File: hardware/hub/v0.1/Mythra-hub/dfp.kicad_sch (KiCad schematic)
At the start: 3 parts, among them J3 918-418K2022C40000

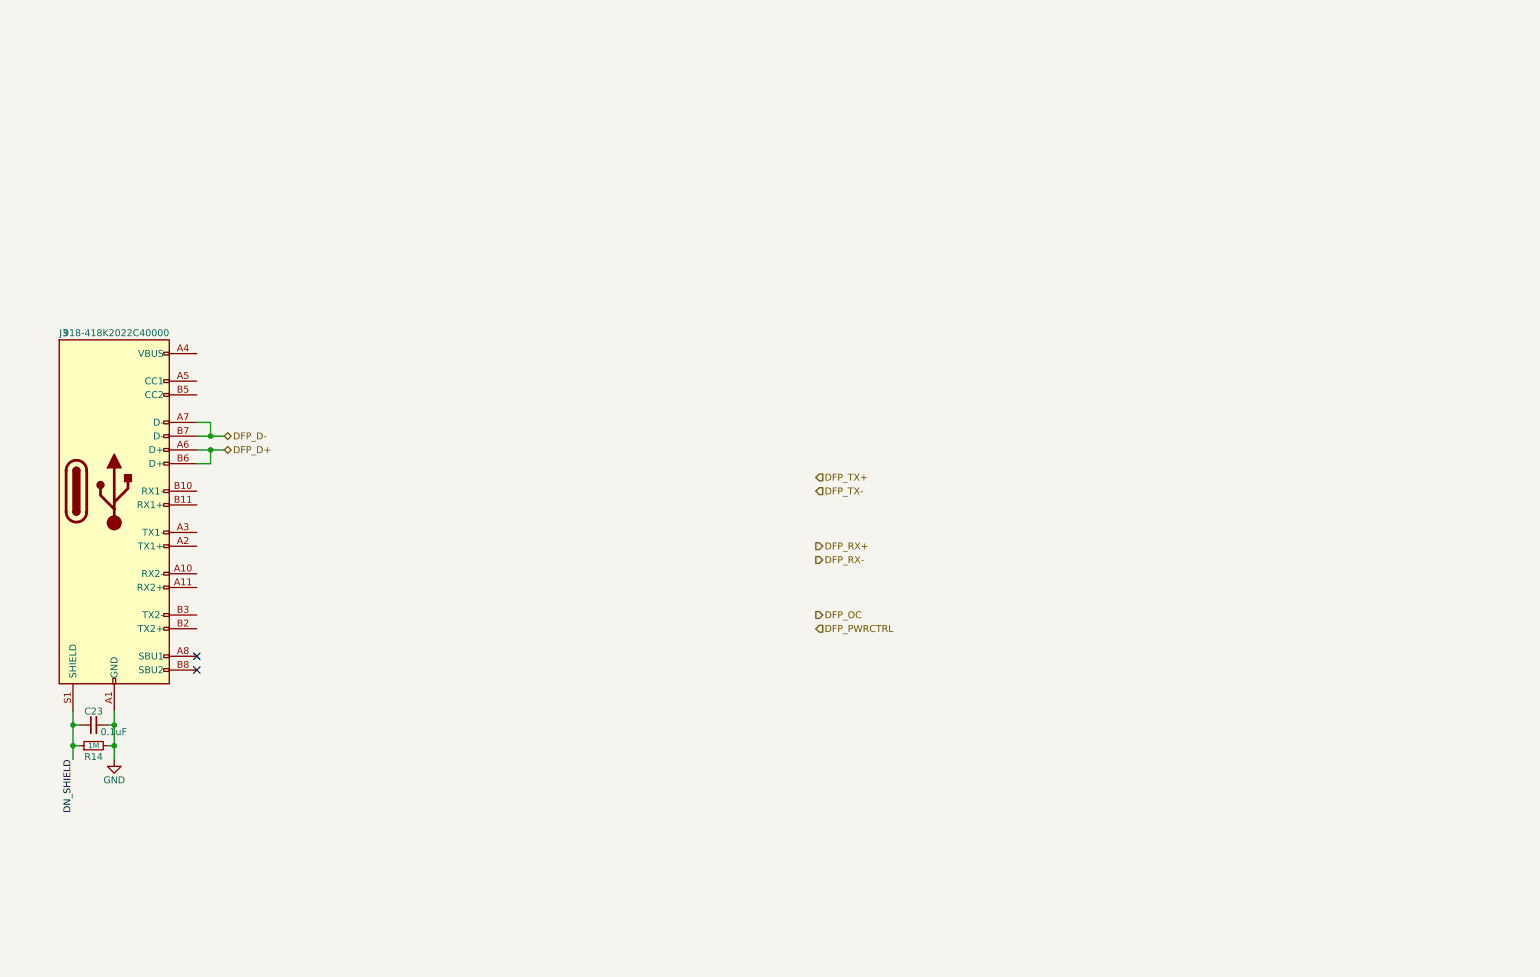
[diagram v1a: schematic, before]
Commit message: Designed the main part of the per-DFP DC-DC
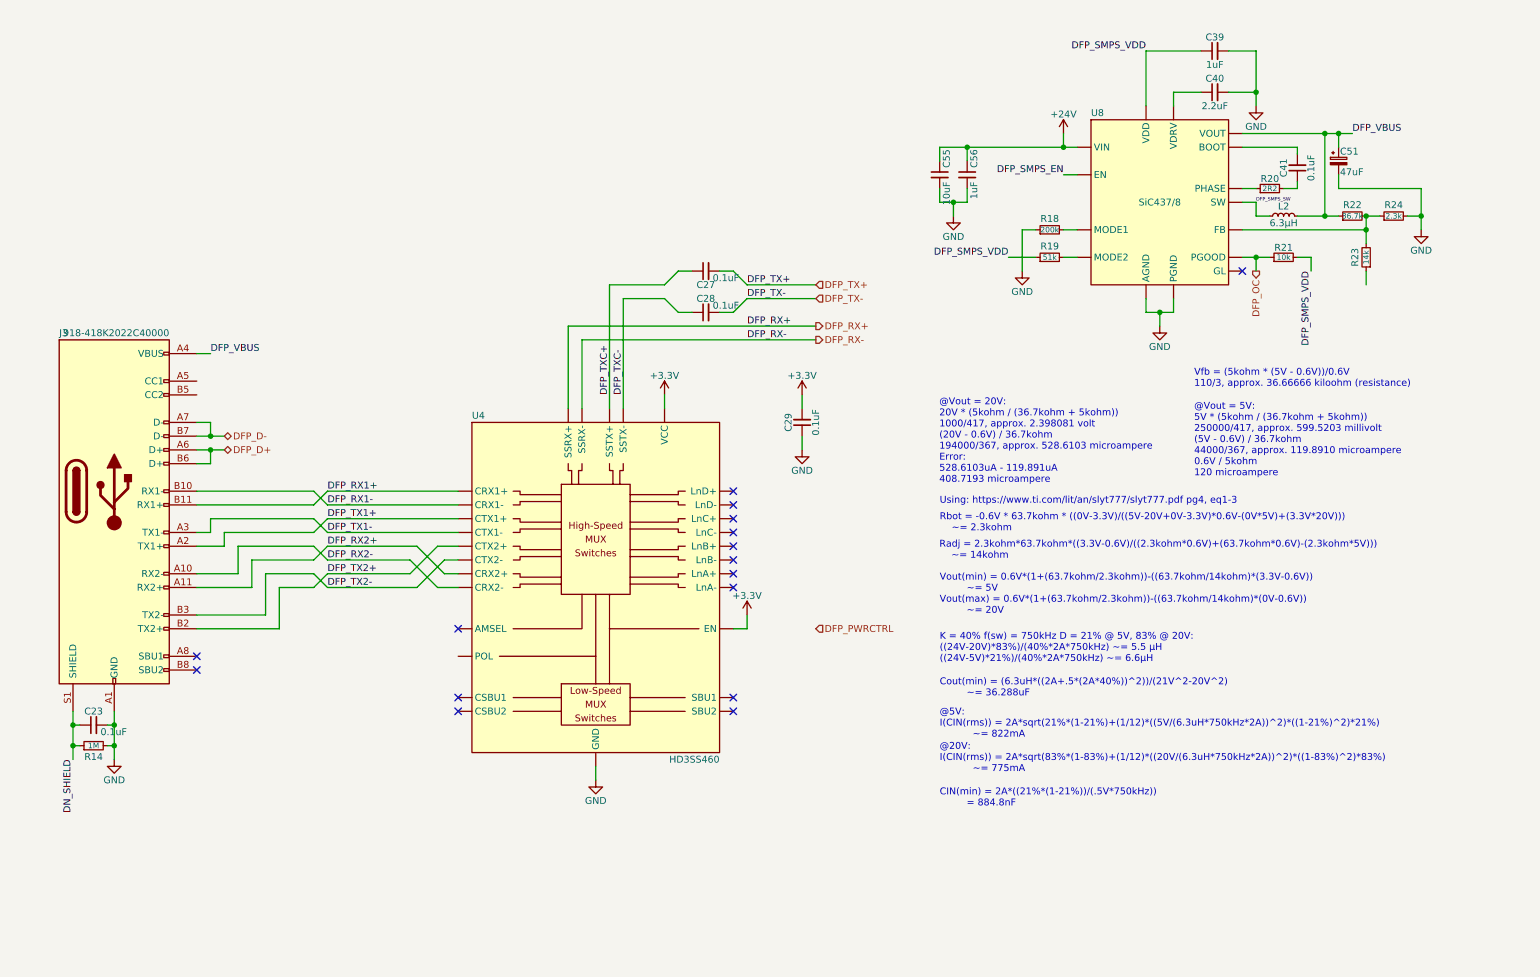
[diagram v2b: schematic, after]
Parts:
- added C27, C28, C29, C41: 0.1uF, rhais_rcl:C0402, symbol Device:C_Small
- added C39: 1uF, rhais_rcl:C0402, symbol Device:C_Small
- added C40: 2.2uF, rhais_rcl:C0402, symbol Device:C_Small
- added C51: 47uF, rhais_rcl:C_Elec_8.3x8.3mm, symbol Device:C_Polarized_Small
- added C55: 10uF, rhais_rcl:C1206, symbol Device:C_Small
- added C56: 1uF, rhais_rcl:C0603, symbol Device:C_Small
- added L2: 6.3µH, rhais_bourns:SRN6045TA, symbol Device:L_Small
- added R18: 200k, rhais_rcl:R0402, symbol Device:R_Small
- added R19: 51k, rhais_rcl:R0402, symbol Device:R_Small
- added R20: 2R2, rhais_rcl:R0402, symbol Device:R_Small
- added R21: 10k, rhais_rcl:R0402, symbol Device:R_Small
- added R22: 36.7k, rhais_rcl:R0402, symbol Device:R_Small
- added R23: 14k, rhais_rcl:R0402, symbol Device:R_Small
- added R24: 2.3k, rhais_rcl:R0402, symbol Device:R_Small
- added U4: HD3SS460, rhais_package-qfn:WQFN-28-1EP_3.5x5.5_P0.5mm_EP2x4mm, symbol DX-MON:HD3SS460
- added U8: SiC437/8, rhais_package-vishay:MLP44-24L, symbol DX-MON:SiC437/8
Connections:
- net DFP_OC: now also R21.1, U8.14 (PGOOD)
- net DFP_RX+: now also U4.28 (SSRX+)
- net DFP_RX-: now also U4.27 (SSRX-)
- net DFP_TX+: now also C27.2
- net DFP_TX-: now also C28.2
- net GND: now also C29.1, C39.2, C40.2, C51.2, C55.2, C56.2, R18.1, R24.2, U4.29 (GND), U8.13 (PGND), U8.16 (AGND), U8.25 (AGND), U8.27 (PGND), U8.3 (PGND), U8.4 (PGND)
- net DFP_RX2-: now reaches J3.A10 (RX2-)
- net DFP_RX2-: now also U4.10 (CRX2-)
- net DFP_RX2+: now reaches J3.A11 (RX2+)
- net DFP_RX2+: now also U4.9 (CRX2+)
- net DFP_TX1+: now reaches J3.A2 (TX1+)
- net DFP_TX1+: now also U4.4 (CTX1+)
- net DFP_TX1-: now reaches J3.A3 (TX1-)
- net DFP_TX1-: now also U4.5 (CTX1-)
- net DFP_VBUS: now reaches J3.A4 (VBUS), J3.A9 (VBUS), J3.B4 (VBUS), J3.B9 (VBUS)
- net DFP_VBUS: now also C51.1, L2.2, R22.1, U8.18 (VOUT)
- net DFP_RX1-: now reaches J3.B10 (RX1-)
- net DFP_RX1-: now also U4.2 (CRX1-)
- net DFP_RX1+: now reaches J3.B11 (RX1+)
- net DFP_RX1+: now also U4.1 (CRX1+)
- net DFP_TX2+: now reaches J3.B2 (TX2+)
- net DFP_TX2+: now also U4.6 (CTX2+)
- net DFP_TX2-: now reaches J3.B3 (TX2-)
- net DFP_TX2-: now also U4.7 (CTX2-)
- new net: U8.10 (GL), U8.11 (GL), U8.28 (GL)
- new net: C40.1, U8.12 (VDRV)
- new net: R22.2, R23.2, R24.1, U8.17 (FB)
- new net: R19.2, U8.20 (MODE2)
- new net: R18.2, U8.21 (MODE1)
- new net: C41.2, U8.23 (BOOT)
- new net: R20.1, U8.24 (PHASE)
- new net: C41.1, R20.2
- new net +24V: C55.1, C56.1, U8.1 (VIN), U8.2 (VIN), U8.22 (VIN)
- new net +3V3: C29.2, U4.17 (EN), U4.22 (VCC)
- new net DFP_SMPS_EN: U8.19 (EN)
- new net DFP_SMPS_SW: L2.1, U8.5 (SW), U8.6 (SW), U8.7 (SW), U8.8 (SW), U8.9 (SW)
- new net DFP_SMPS_VDD: C39.1, R19.1, R21.2, U8.15 (VDD)
- new net DFP_TXC+: C27.1, U4.26 (SSTX+)
- new net DFP_TXC-: C28.1, U4.25 (SSTX-)
- no-connect marks 2 -> 16
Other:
- note added: "@20V: I(CIN(rms)) = 2A*sqrt(83%*(1-83%)+(1/12)*((20V/(6.3uH*750kHz*2A))^2)*((1-83%)^2)*83%) ~= 775mA"
- note added: "@5V: I(CIN(rms)) = 2A*sqrt(21%*(1-21%)+(1/12)*((5V/(6.3uH*750kHz*2A))^2)*((1-21%)^2)*21%) ~= 822mA"
- note added: "@Vout = 20V: 20V * (5kohm / (36.7kohm + 5kohm)) 1000/417, approx. 2.398081 volt (20V - 0.6V) / 36.7kohm 194000/367, approx. 528.6103 microampere Error: 528.6103uA - 119.891uA 408.7193 microampere"
- note added: "@Vout = 5V: 5V * (5kohm / (36.7kohm + 5kohm)) 250000/417, approx. 599.5203 millivolt (5V - 0.6V) / 36.7kohm 44000/367, approx. 119.8910 microampere 0.6V / 5kohm 120 microampere"
- note added: "CIN(min) = 2A*((21%*(1-21%))/(.5V*750kHz)) = 884.8nF"
- note added: "Cout(min) = (6.3uH*((2A+.5*(2A*40%))^2))/(21V^2-20V^2) ~= 36.288uF"
- note added: "K = 40% f(sw) = 750kHz D = 21% @ 5V, 83% @ 20V: ((24V-20V)*83%)/(40%*2A*750kHz) ~= 5.5 µH ((24V-5V)*21%)/(40%*2A*750kHz) ~= 6.6µH"
- note added: "Radj = 2.3kohm*63.7kohm*((3.3V-0.6V)/((2.3kohm*0.6V)+(63.7kohm*0.6V)-(2.3kohm*5V))) ~= 14kohm"
- note added: "Rbot = -0.6V * 63.7kohm * ((0V-3.3V)/((5V-20V+0V-3.3V)*0.6V-(0V*5V)+(3.3V*20V))) ~= 2.3kohm"
- note added: "Using: https://www.ti.com/lit/an/slyt777/slyt777.pdf pg4, eq1-3"
- note added: "Vfb = (5kohm * (5V - 0.6V))/0.6V 110/3, approx. 36.66666 kiloohm (resistance)"
- note added: "Vout(min) = 0.6V*(1+(63.7kohm/2.3kohm))-((63.7kohm/14kohm)*(3.3V-0.6V)) ~= 5V Vout(max) = 0.6V*(1+(63.7kohm/2.3kohm))-((63.7kohm/14kohm)*(0V-0.6V)) ~= 20V"

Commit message: part information cleanup in the DFP schematic
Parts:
- R20: MFR Yageo -> Multicomp; MPN RC0402FR-0710KL -> MCWR04W2R20FTL; OC_FARNELL (none) -> 2447154; OC_LCSC C60490 -> (none); URL_FARNELL (none) -> https://uk.farnell.com/multicomp/mcwr04w2r20ftl/res-2r2-1-0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; URL_LCSC https://lcsc.com/product-detail/Chip-Resistor-Surface-Mount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 -> (none)
- R22: MFR (none) -> Walsin; MPN (none) -> WR04X3652FTL; OC_FARNELL (none) -> 2668216; URL_FARNELL (none) -> https://uk.farnell.com/walsin/wr04x3652ftl/res-36k5-1-0-062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
- R23: MFR (none) -> Multicomp; MPN (none) -> MCWR04X1402FTL; OC_FARNELL (none) -> MCWR04X1402FTL; URL_FARNELL (none) -> https://uk.farnell.com/multicomp/mcwr04x1402ftl/res-14k-1-0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
- R24: MFR (none) -> Multicomp Pro; MPN (none) -> MCWR04X2321FTL; OC_FARNELL (none) -> 2694571; URL_FARNELL (none) -> https://uk.farnell.com/multicomp/mcwr04x2321ftl/res-2k32-1-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
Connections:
- net +24V: now also U8.26 (VIN)
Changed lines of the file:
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@@
       (effects (font (size 1.27 1.27)) hide)
     )
-    (property "Datasheet" "https://datasheet.lcsc.com/lcsc/1809301715_YAGEO-RC0402FR-0710KL_C60490.pdf" (id 3) (at 248.92 48.26 0)
-      (effects (font (size 1.27 1.27)) hide)
-    )
-    (property "MFR" "Yageo" (id 4) (at 248.92 48.26 0)
-      (effects (font (size 1.27 1.27)) hide)
-    )
-    (property "MPN" "RC0402FR-0710KL" (id 5) (at 248.92 48.26 0)
-      (effects (font (size 1.27 1.27)) hide)
-    )
-    (property "OC_LCSC" "C60490" (id 6) (at 248.92 48.26 0)
-      (effects (font (size 1.27 1.27)) hide)
-    )
-    (property "URL_LCSC" "https://lcsc.com/product-detail/Chip-Resistor-Surface-Mount_YAGEO-RC0402FR-0710KL_C60490.html" (id 7) (at 248.92 48.26 0)
+    (property "Datasheet" "https://www.farnell.com/datasheets/2860681.pdf" (id 3) (at 248.92 48.26 0)
+      (effects (font (size 1.27 1.27)) hide)
+    )
+    (property "MFR" "Multicomp" (id 4) (at 248.92 48.26 0)
+      (effects (font (size 1.27 1.27)) hide)
+    )
+    (property "MPN" "MCWR04W2R20FTL" (id 5) (at 248.92 48.26 0)
+      (effects (font (size 1.27 1.27)) hide)
+    )
+    (property "OC_FARNELL" "2447154" (id 6) (at 248.92 48.26 90)
+      (effects (font (size 1.27 1.27)) hide)
+    )
+    (property "URL_FARNELL" "https://uk.farnell.com/multicomp/mcwr04w2r20ftl/res-2r2-1-0-0625w-thick-film/dp/2447154" (id 7) (at 248.92 48.26 90)
       (effects (font (size 1.27 1.27)) hide)
     )
@@
       (effects (font (size 1.27 1.27)) hide)
     )
-    (property "Datasheet" "~" (id 3) (at 264.16 53.34 0)
+    (property "Datasheet" "http://www.passivecomponent.com/wp-content/uploads/chipR/ASC_WR.pdf" (id 3) (at 264.16 53.34 0)
+      (effects (font (size 1.27 1.27)) hide)
+    )
+    (property "MFR" "Walsin" (id 4) (at 264.16 53.34 90)
+      (effects (font (size 1.27 1.27)) hide)
+    )
+    (property "MPN" "WR04X3652FTL" (id 5) (at 264.16 53.34 90)
+      (effects (font (size 1.27 1.27)) hide)
+    )
+    (property "OC_FARNELL" "2668216" (id 6) (at 264.16 53.34 90)
+      (effects (font (size 1.27 1.27)) hide)
+    )
+    (property "URL_FARNELL" "https://uk.farnell.com/walsin/wr04x3652ftl/res-36k5-1-0-0625w-0402-thick/dp/2668216" (id 7) (at 264.16 53.34 90)
       (effects (font (size 1.27 1.27)) hide)
     )
@@
       (effects (font (size 1.27 1.27)) hide)
     )
-    (property "Datasheet" "~" (id 3) (at 266.7 60.96 0)
+    (property "Datasheet" "https://www.farnell.com/datasheets/2860681.pdf" (id 3) (at 266.7 60.96 0)
+      (effects (font (size 1.27 1.27)) hide)
+    )
+    (property "MFR" "Multicomp" (id 4) (at 266.7 60.96 90)
+      (effects (font (size 1.27 1.27)) hide)
+    )
+    (property "MPN" "MCWR04X1402FTL" (id 5) (at 266.7 60.96 90)
+      (effects (font (size 1.27 1.27)) hide)
+    )
+    (property "OC_FARNELL" "MCWR04X1402FTL" (id 6) (at 266.7 60.96 90)
+      (effects (font (size 1.27 1.27)) hide)
+    )
+    (property "URL_FARNELL" "https://uk.farnell.com/multicomp/mcwr04x1402ftl/res-14k-1-0-0625w-thick-film/dp/2447109" (id 7) (at 266.7 60.96 90)
       (effects (font (size 1.27 1.27)) hide)
     )
@@
       (effects (font (size 1.27 1.27)) hide)
     )
-    (property "Datasheet" "~" (id 3) (at 271.78 53.34 0)
+    (property "Datasheet" "https://www.farnell.com/datasheets/2189593.pdf" (id 3) (at 271.78 53.34 0)
+      (effects (font (size 1.27 1.27)) hide)
+    )
+    (property "MFR" "Multicomp Pro" (id 4) (at 271.78 53.34 90)
+      (effects (font (size 1.27 1.27)) hide)
+    )
+    (property "MPN" "MCWR04X2321FTL" (id 5) (at 271.78 53.34 90)
+      (effects (font (size 1.27 1.27)) hide)
+    )
+    (property "OC_FARNELL" "2694571" (id 6) (at 271.78 53.34 90)
+      (effects (font (size 1.27 1.27)) hide)
+    )
+    (property "URL_FARNELL" "https://uk.farnell.com/multicomp/mcwr04x2321ftl/res-2k32-1-0-0625w-0402-thick/dp/2694571" (id 7) (at 271.78 53.34 90)
       (effects (font (size 1.27 1.27)) hide)
     )
@@
     (pin "24")
     (pin "25")
+    (pin "26")
     (pin "27")
     (pin "28")
